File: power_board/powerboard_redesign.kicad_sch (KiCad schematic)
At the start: 20 parts, among them J1 Conn_01x04_Pin, J2 282834-2, J3 282834-2, J4 282834-2, J5 BM06B-SRSS-TBLFSN, J6 B4B-XH-A, J7 282834-2, U1 PDQ30-Q24-S12-D

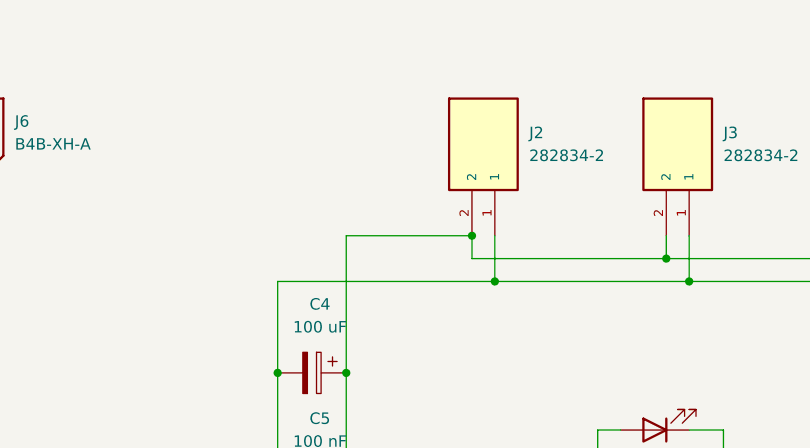
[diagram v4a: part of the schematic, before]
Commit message: Added 28 awg terminal block to schematic
This is for LiDAR connection power wires as another option instead of JST 6-pin connector
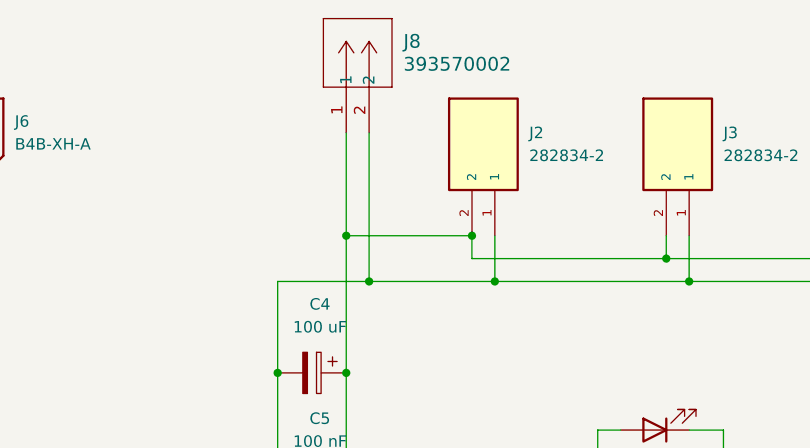
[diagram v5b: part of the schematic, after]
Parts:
- added J8: 393570002, F1TenthPowerBoard:CONN_SD-39357-001_02P_MOL, symbol CONN_SD-39357-001_02P_MOL:393570002
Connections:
- net at C1.1, C4.1, C5.1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: now also J8.1
- net at C1.2, C4.2, C5.2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: now also J8.2
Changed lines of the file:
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@@
+	)
+	(junction
+		(at 165.1 53.34)
+		(diameter 0)
+		(color 0 0 0 0)
 	)
 	(junction
 		(at 102.87 106.68)
+		(diameter 0)
+		(color 0 0 0 0)
+	)
+	(junction
+		(at 167.64 58.42)
 		(diameter 0)
 		(color 0 0 0 0)
@@
 	(wire
 		(pts
+			(xy 167.64 41.91) (xy 167.64 58.42)
+		)
+		(stroke
+			(width 0)
+			(type default)
+		)
+	)
+	(wire
+		(pts
 			(xy 110.49 106.68) (xy 120.65 106.68)
 		)
@@
 	(wire
 		(pts
+			(xy 165.1 41.91) (xy 165.1 53.34)
+		)
+		(stroke
+			(width 0)
+			(type default)
+		)
+	)
+	(wire
+		(pts
 			(xy 241.3 50.8) (xy 241.3 64.77)
 		)
@@
 	(wire
 		(pts
+			(xy 167.64 58.42) (xy 157.48 58.42)
+		)
+		(stroke
+			(width 0)
+			(type default)
+		)
+	)
+	(wire
+		(pts
 			(xy 102.87 91.44) (xy 102.87 106.68)
 		)
@@
 	(wire
 		(pts
-			(xy 181.61 58.42) (xy 157.48 58.42)
+			(xy 181.61 58.42) (xy 167.64 58.42)
 		)
 		(stroke
@@
 					(unit 1)
 				)
+			)
+		)
+	)
+	(symbol
+		(lib_id "CONN_SD-39357-001_02P_MOL:393570002")
+		(at 165.1 41.91 90)
+		(unit 1)
+		(exclude_from_sim no)
+		(in_bom yes)
+		(on_board yes)
+		(dnp no)
+		(fields_autoplaced yes)
+		(property "Reference" "J8"
+			(at 171.45 31.7499 90)
+			(effects
+				(font
+					(size 1.524 1.524)
+				)
+				(justify right)
+			)
+		)
+		(property "Value" "393570002"
+			(at 171.45 34.2899 90)
+			(effects
+				(font
+					(size 1.524 1.524)
+				)
+				(justify right)
+			)
+		)
+		(property "Footprint" "F1TenthPowerBoard:CONN_SD-39357-001_02P_MOL"
+			(at 165.1 41.91 0)
+			(effects
+				(font
+					(size 1.27 1.27)
+					(italic yes)
+				)
+				(hide yes)
+			)
+		)
+		(property "Datasheet" "https://www.molex.com/en-us/products/part-detail-pdf/393570002?display=pdf"
+			(at 165.1 41.91 0)
+			(effects
+				(font
+					(size 1.27 1.27)
+					(italic yes)
+				)
+				(hide yes)
+			)
+		)
+		(property "Description" ""
+			(at 165.1 41.91 0)
+			(effects
+				(font
+					(size 1.27 1.27)
+				)
+				(hide yes)
+			)
+		)
+		(pin "1"
+		)
+		(pin "2"
+		)
+		(instances
+			(project ""
+				(path "/730a7e3b-debe-415e-92d1-0c8950d2c05d"
+					(reference "J8")
+					(unit 1)
+				)
